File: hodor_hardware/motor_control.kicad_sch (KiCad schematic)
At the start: 78 parts, among them J6 Screw_Terminal_01x04, J7 Screw_Terminal_01x02, Q5 BSS138, Q7 SiS443DN, Q8 2V7002, T15 I_SNS, T16 D_FB, T17 D_PWM2, T18 D_PWM1, T19 VC_OUT, T20 V_LDSNS, T22 VC_CMP, T23 VC_REF, T25 DRV_EN, T26 DRV_SF, T27 SF_Q, T28 SF_TRG, T29 SF_CLR, T30 ENC_B, T31 ENC_A, U11 MCP6561x-LT, U12 MC33HB2002, U13 74LVC1G123, U14 ACS722xLCTR-10AB, U7 74LVC2G14, U8 ZXTR2105F

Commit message: Schematic finished
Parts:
- added U10: LM4040DBZ-2.5, Package_TO_SOT_SMD:SOT-23, symbol Reference_Voltage:LM4040DBZ-2.5
- C37, C47, C48, C50: value 100n -> 100nF
- J6: footprint (none) -> TerminalBlock_Phoenix:TerminalBlock_Phoenix_PT-1,5-4-3.5-H_1x04_P3.50mm_Horizontal
- J7: footprint (none) -> TerminalBlock_Phoenix:TerminalBlock_Phoenix_PT-1,5-2-3.5-H_1x02_P3.50mm_Horizontal
- JP1: footprint (none) -> Jumper:SolderJumper-2_P1.3mm_Bridged_Pad1.0x1.5mm
- R40: value 20k -> 1k
- R45: value 20k -> 10k
- R65: value 100 -> 100R
- T15, T16, T17, T18, T19, T20, T22, T23, T25, T26, T27, T28, T29, T30, T31: now left out of the parts list
- U7: footprint (none) -> Package_TO_SOT_SMD:SOT-23-6
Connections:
- net AGND: now also U10.2 (A)
- net at R40.2, R45.1, T23.1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: now also U10.1 (K)
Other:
- note added: "Brake chopper (Burns voltage peaks at a load resistor) - Activates at voltages > 27 V (V_REF > 2.5 V) - Independent of main supply, if power is off and motor works as generator - Can be deactivated by opening jumper"
- note removed: "Brake chopper (Burns voltage peaks at a load resistor) - Activates at voltages > 26.5 V (V_REF > 2.5 V) - Independent of main supply, if power is off and motor works as generator - Can be deactivated by opening jumper"
- moved on the sheet: D23, Q5, Q7, R37, R38, R43, R44, R47, R48, R49, T19, T22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

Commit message: Reworked into 2 PCBs
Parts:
- J7: footprint TerminalBlock_Phoenix:TerminalBlock_Phoenix_PT-1,5-2-3.5-H_1x02_P3.50mm_Horizontal -> TerminalBlock_Phoenix:TerminalBlock_Phoenix_MKDS-1,5-2_1x02_P5.00mm_Horizontal
- R37: value 1k -> 10k; footprint Resistor_SMD:R_0805_2012Metric -> Resistor_SMD:R_0402_1005Metric
- R38: value 1.5k -> 2k
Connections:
- net at C53.1, L11.2: now also J7.2 (Pin_2); no longer J7.1 (Pin_1)
- net at C52.2, L12.2: now also J7.1 (Pin_1); no longer J7.2 (Pin_2)
- net ~{CS} renamed ~{CS0}
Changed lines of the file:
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@@
 	)
 	(bus_alias "SPI"
-		(members "MISO" "MOSI" "~{CS}" "SCK")
+		(members "MISO" "MOSI" "~{CS0}" "SCK" "~{CS1}")
 	)
 	(text "Brake chopper (Burns voltage peaks at a load resistor)\n- Activates at voltages > 27 V (V_REF > 2.5 V)\n- Independent of main supply, if power is off and motor works as generator\n- Can be deactivated by opening jumper"
@@
 	)
 	(junction
-		(at 60.96 81.28)
-		(diameter 0)
-		(color 0 0 0 0)
-	)
-	(junction
 		(at 33.655 43.18)
 		(diameter 0)
@@
 	)
 	(junction
+		(at 60.96 81.28)
+		(diameter 0)
+		(color 0 0 0 0)
+	)
+	(junction
 		(at 35.56 66.04)
 		(diameter 0)
@@
 	)
 	(bus_entry
-		(at 46.355 83.82)
+		(at 46.355 78.74)
 		(size 2.54 -2.54)
 		(stroke
@@
 	)
 	(bus_entry
-		(at 46.355 78.74)
+		(at 46.355 83.82)
 		(size 2.54 -2.54)
 		(stroke
@@
 	(wire
 		(pts
-			(xy 48.895 81.28) (xy 60.96 81.28)
-		)
-		(stroke
-			(width 0)
-			(type default)
-		)
-	)
-	(wire
-		(pts
 			(xy 200.025 73.66) (xy 200.025 72.39)
 		)
@@
 	(wire
 		(pts
+			(xy 48.895 81.28) (xy 60.96 81.28)
+		)
+		(stroke
+			(width 0)
+			(type default)
+		)
+	)
+	(wire
+		(pts
 			(xy 178.435 115.57) (xy 184.785 115.57)
 		)
@@
 		)
 	)
-	(label "~{CS}"
-		(at 54.61 81.28 0)
-		(effects
-			(font
-				(size 1.27 1.27)
-			)
-			(justify left bottom)
-		)
-	)
 	(label "OUT2"
 		(at 102.235 38.735 0)
@@
 		)
 	)
+	(label "~{CS0}"
+		(at 54.61 81.28 0)
+		(effects
+			(font
+				(size 1.27 1.27)
+			)
+			(justify left bottom)
+		)
+	)
 	(label "DRV_DIS"
 		(at 27.94 63.5 180)
@@
 			)
 		)
-		(property "Value" "1.5k"
+		(property "Value" "2k"
 			(at 256.413 61.468 0)
 			(effects
@@
 			)
 		)
-		(property "Value" "1k"
+		(property "Value" "10k"
 			(at 256.413 48.133 0)
 			(effects
@@
 			)
 		)
-		(property "Footprint" "Resistor_SMD:R_0805_2012Metric"
+		(property "Footprint" "Resistor_SMD:R_0402_1005Metric"
 			(at 252.857 46.99 90)
 			(effects
@@
 	(symbol
 		(lib_id "Connector:Screw_Terminal_01x02")
-		(at 138.43 69.85 0)
+		(at 138.43 72.39 0)
+		(mirror x)
 		(unit 1)
 		(exclude_from_sim no)
@@
 		(dnp no)
 		(property "Reference" "J7"
-			(at 137.795 66.675 0)
+			(at 137.795 75.565 0)
 			(effects
 				(font
@@
 		)
 		(property "Value" "Screw_Terminal_01x02"
-			(at 142.24 73.66 90)
+			(at 142.24 68.58 90)
 			(effects
 				(font
@@
 			)
 		)
-		(property "Footprint" "TerminalBlock_Phoenix:TerminalBlock_Phoenix_PT-1,5-2-3.5-H_1x02_P3.50mm_Horizontal"
-			(at 138.43 69.85 0)
+		(property "Footprint" "TerminalBlock_Phoenix:TerminalBlock_Phoenix_MKDS-1,5-2_1x02_P5.00mm_Horizontal"
+			(at 138.43 72.39 0)
 			(effects
 				(font
@@
 		)
 		(property "Datasheet" "~"
-			(at 138.43 69.85 0)
+			(at 138.43 72.39 0)
 			(effects
 				(font
@@
 		)
 		(property "Description" "Generic screw terminal, single row, 01x02, script generated (kicad-library-utils/schlib/autogen/connector/)"
-			(at 138.43 69.85 0)
+			(at 138.43 72.39 0)
 			(effects
 				(font
@@
 		)
 		(instances
-			(project ""
+			(project "hodor_hardware"
 				(path "/2da01e60-41ef-423d-82f4-a5c8908d8b96/d9462714-63c5-4d20-a6ea-aefea568c44f"
 					(reference "J7")

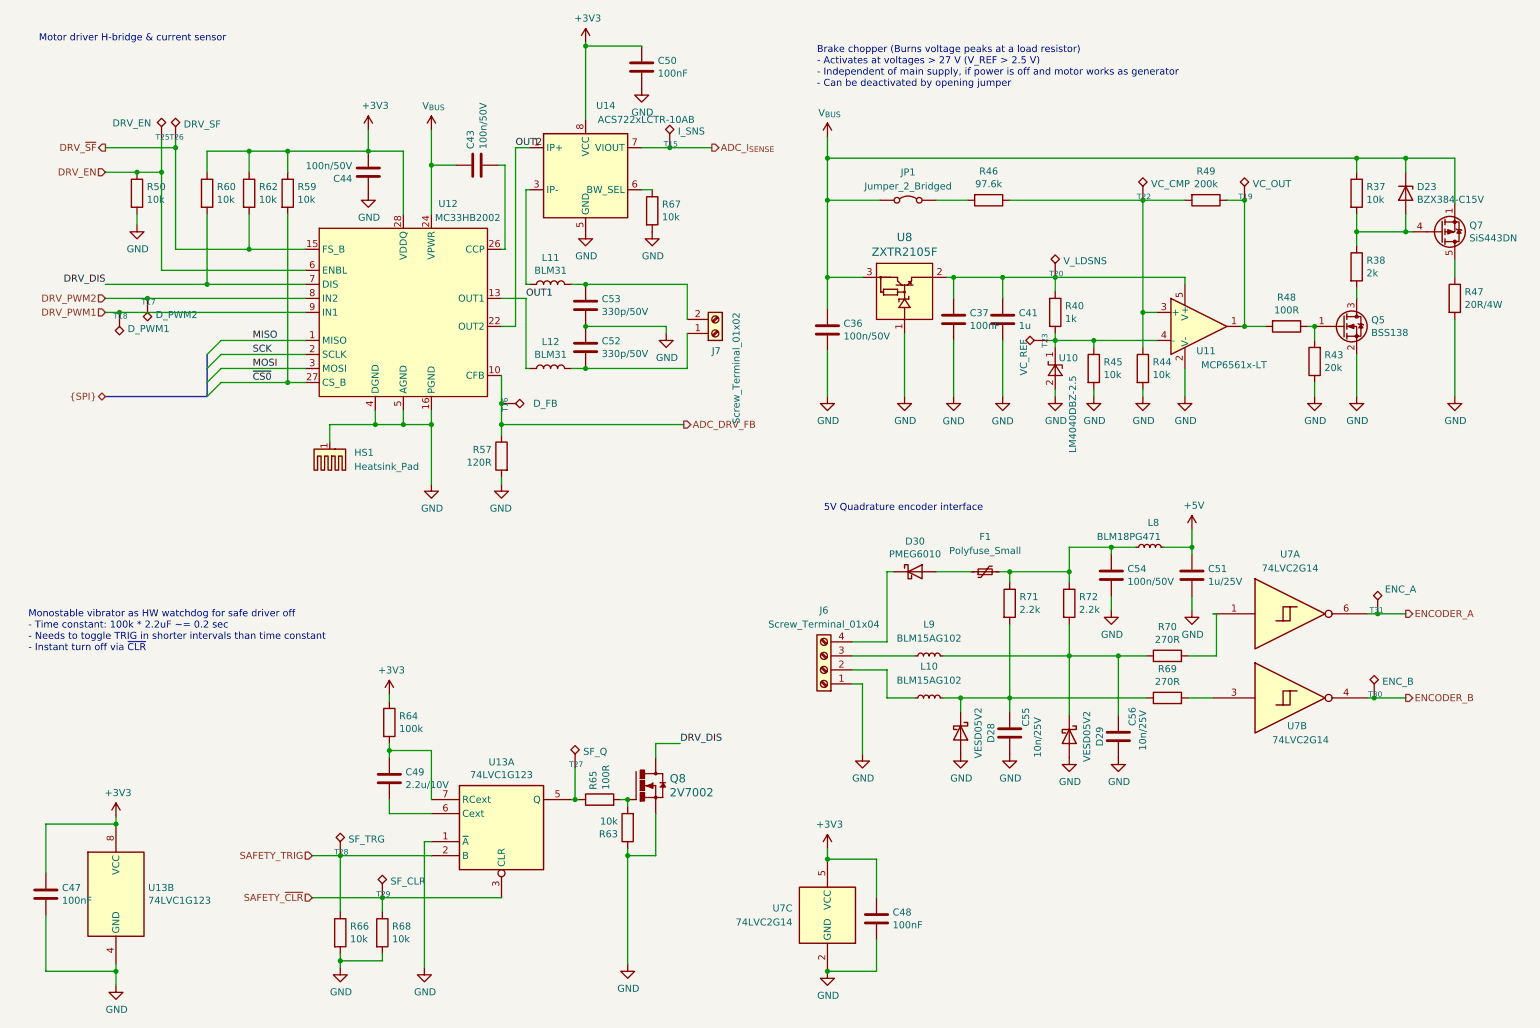
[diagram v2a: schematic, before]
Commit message: Finished schematic and initial placement on PCB
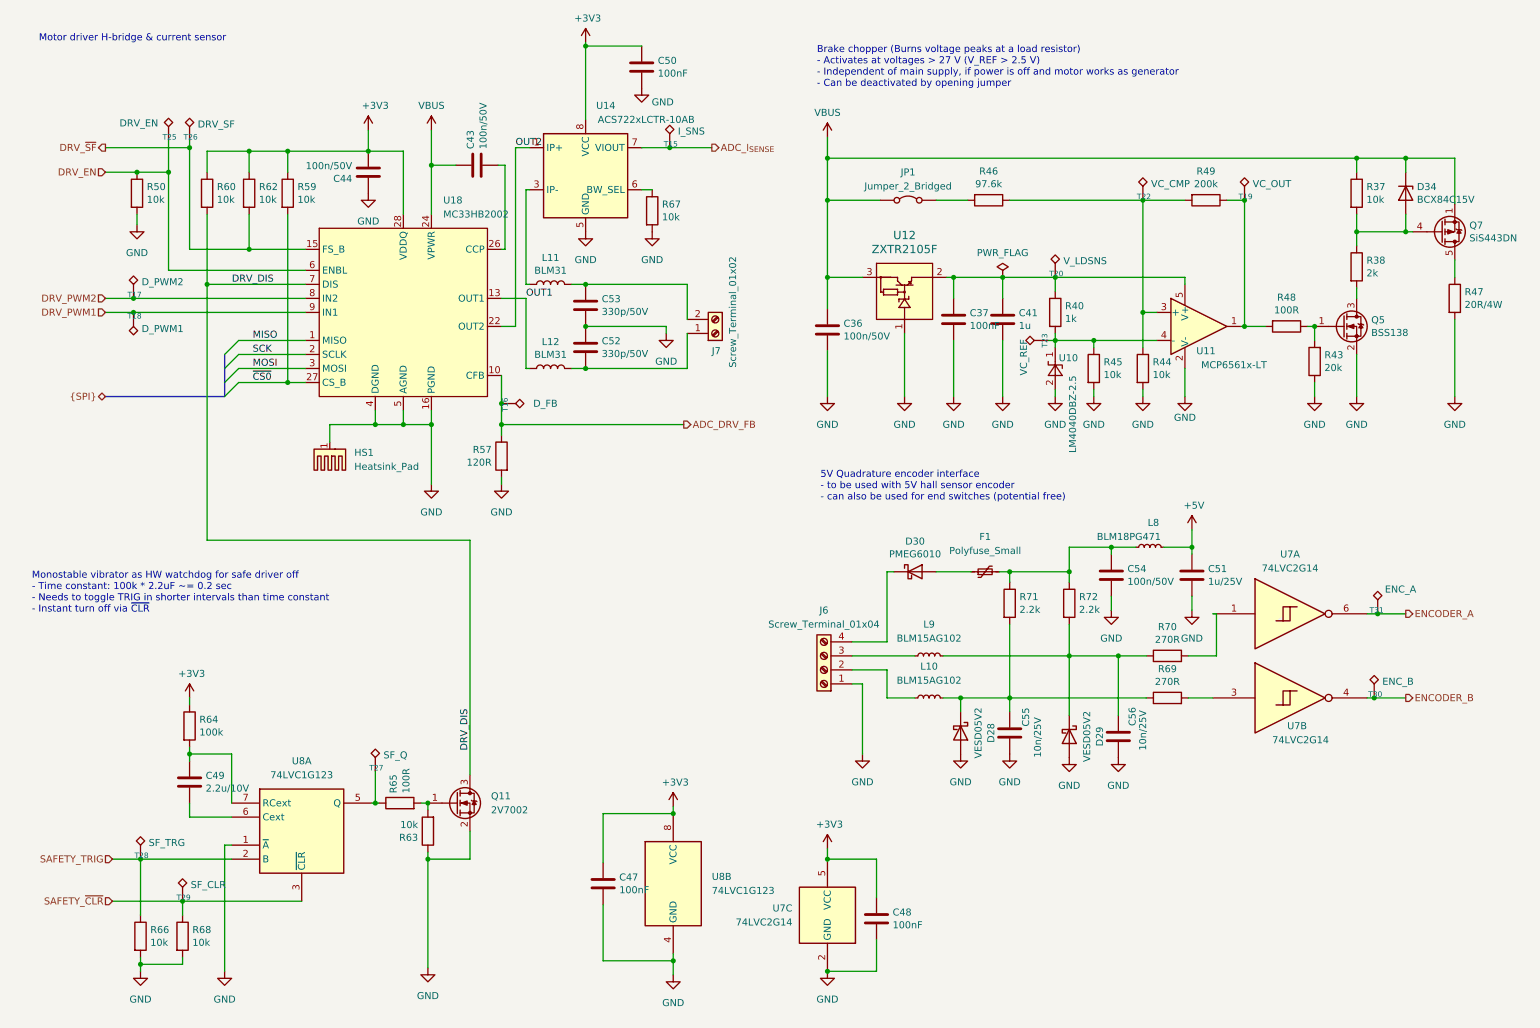
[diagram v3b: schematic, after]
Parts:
- removed D23: BZX384-C15V, Diode_SMD:D_SOD-323, symbol Hodor-rescue:BZX384-xxx-Diode
- removed Q8: 2V7002, Package_TO_SOT_SMD:SOT-323_SC-70, symbol Hodor-rescue:FDY301NZ-00_MM_Parts
- removed U12: MC33HB2002, mm_parts_footprints:HVQFN-28-1EP_6x6mm_MC33HB2002, symbol mm_parts:MC33HB2002
- removed U13: 74LVC1G123, Package_SO:MSOP-8_3x3mm_P0.65mm, symbol Hodor-rescue:74LVC1G123-74xGxx
- removed U8: ZXTR2105F, Package_TO_SOT_SMD:SOT-23, symbol Hodor-rescue:ZXTR2105F-00_MM_Parts
- added D34: BCX84C15V, Diode_SMD:D_SOD-523, symbol Device:D_Zener
- added Q11: 2V7002, Package_TO_SOT_SMD:SOT-323_SC-70, symbol Transistor_FET:Si1308EDL
- added U12: ZXTR2105F, Package_TO_SOT_SMD:SOT-23, symbol hodor_custom_parts:ZXTR2105F
- added U18: MC33HB2002, hodor_footprints:HVQFN-28-1EP_6x6mm_MC33HB2002, symbol hodor_custom_parts:MC33HB2002
- added U8: 74LVC1G123, Package_SO:VSSOP-8_2.3x2mm_P0.5mm, symbol 74xGxx:74LVC1G123
- J6: footprint TerminalBlock_Phoenix:TerminalBlock_Phoenix_PT-1,5-4-3.5-H_1x04_P3.50mm_Horizontal -> TerminalBlock_Phoenix:TerminalBlock_Phoenix_MKDS-1,5-4_1x04_P5.00mm_Horizontal
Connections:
- net +3V3: now also U18.28 (VDDQ), U8.8 (VCC)
- net ADC_DRV_FB: now also U18.10 (CFB)
- net AGND: now also Q11.2 (S), U12.1 (GND), U18.16 (PGND), U18.17 (PGND), U18.18 (PGND), U18.19 (PGND), U18.20 (PGND), U18.21 (AGND), U18.29 (AGND), U18.4 (DGND), U18.5 (AGND), U8.1 (~{A}), U8.4 (GND)
- net DRV_DIS: now also Q11.3 (D), U18.7 (DIS)
- net DRV_EN: now also U18.6 (ENBL)
- net DRV_PWM1: now also U18.9 (IN1)
- net DRV_PWM2: now also U18.8 (IN2)
- net DRV_~{SF}: now also U18.15 (FS_B)
- net MISO: now also U18.1 (MISO)
- net MOSI: now also U18.3 (MOSI)
- net OUT1: now also U18.13 (OUT1), U18.14 (OUT1)
- net OUT2: now also U18.22 (OUT2), U18.23 (OUT2)
- net SAFETY_TRIG: now also U8.2 (B)
- net SAFETY_~{CLR}: now also U8.3 (~{CLR})
- net SCK: now also U18.2 (SCLK)
- net ~{CS0}: now also U18.27 (CS_B)
- net at C37.1, C41.1, R40.1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: now also U12.2 (VOUT)
- net at Q7.4 (G), R37.2, R38.1: now also D34.2 (A)
- net at R65.1, T27.1: now also U8.5 (Q)
- net at C49.2: now also U8.6 (Cext)
- net at C49.1, R64.2: now also U8.7 (RCext)
- net at R63.2, R65.2: now also Q11.1 (G)
- net at C43.2: now also U18.26 (CCP)
- net VPWR renamed VBUS
- net VBUS: now also D34.1 (K), U12.3 (VIN), U18.11 (VPWR), U18.12 (VPWR), U18.24 (VPWR), U18.25 (VPWR)
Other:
- note added: "5V Quadrature encoder interface - to be used with 5V hall sensor encoder - can also be used for end switches (potential free)"
- note removed: "5V Quadrature encoder interface"
- moved on the sheet: C47, C49, R63, R64, R65, R66, R68, T17, T18, T25, T26, T27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

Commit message: Latest changes
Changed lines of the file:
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@@
 	)
 	(junction
+		(at 93.98 167.64)
+		(diameter 0)
+		(color 0 0 0 0)
+	)
+	(junction
 		(at 39.37 43.18)
 		(diameter 0)
@@
 	)
 	(junction
-		(at 86.36 167.64)
-		(diameter 0)
-		(color 0 0 0 0)
-	)
-	(junction
 		(at 99.695 88.9)
 		(diameter 0)
@@
 	(wire
 		(pts
-			(xy 86.36 167.64) (xy 86.36 187.325)
+			(xy 93.98 167.64) (xy 93.98 187.325)
 		)
 		(stroke
@@
 	(symbol
 		(lib_id "power:GND")
-		(at 86.36 187.325 0)
+		(at 93.98 187.325 0)
 		(unit 1)
 		(exclude_from_sim no)
@@
 		(fields_autoplaced yes)
 		(property "Reference" "#PWR0109"
-			(at 86.36 193.675 0)
+			(at 93.98 193.675 0)
 			(effects
 				(font
@@
 		)
 		(property "Value" "GND"
-			(at 86.36 192.405 0)
+			(at 93.98 192.405 0)
 			(effects
 				(font
@@
 		)
 		(property "Footprint" ""
-			(at 86.36 187.325 0)
+			(at 93.98 187.325 0)
 			(effects
 				(font
@@
 		)
 		(property "Datasheet" ""
-			(at 86.36 187.325 0)
+			(at 93.98 187.325 0)
 			(effects
 				(font
@@
 		)
 		(property "Description" "Power symbol creates a global label with name \"GND\" , ground"
-			(at 86.36 187.325 0)
+			(at 93.98 187.325 0)
 			(effects
 				(font
